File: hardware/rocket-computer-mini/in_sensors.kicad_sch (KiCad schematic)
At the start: 20 parts, among them J8 CON-SMA-EDGE-S, U16 E220-900MM22S, U2 ISM6HG256XTR, U3 IIS2MDCTR, U4 BMP585, U5 LC86GLAMD

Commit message: hardware(minis): cost-reduction part swaps (Tier A + USB-C + QMC5883P)
rocket-computer-mini:
- pyro high-side P-FETs U6-U10: TPN4R712MD -> Winsok WSD20L50DN33 (incumbent
  unbuyable at build qty until the Q4-2026 Mouser restock; land compatibility
  closed by numeric overlay of the vendor package drawing vs the TSON Advance
  land vs the Toshiba outline -- identical 0.202 mm bottom-metal overlap;
  first-article gate: end-face wetting + bench-fire)
- pyro-ARM N-FET U9: CSD16323Q3 -> AOS AON7534 (same pinout, land verified)
- gate drivers Q3-Q6: DTC123JEBTL -> DTC123JETL (SOT-416 leads land fully)
- battery shunt R72: CSSH0805FT2L00 -> Yageo PA0805FRF870R002L
- magnetometer U3: IIS2MDC -> QST QMC5883P (new Custom symbol + LGA-16 3x3
  footprint from the vendor land; U3 relocated, C2/C4/C6 re-arranged; C6
  220 nF -> 4.7 uF 16 V 0603 for the C1 reservoir; 2x2 mm all-layer no-pour
  rule area under the die; stale X/Y axis silk removed -- new markings when
  the firmware axis mapping is decided; needs a new ~10-register driver)
- USB-C stays GCT: the HRO's through-hole shell legs land inside the pyro
  terminal's back-side SMD pads -- physically blocked at this location

base-station-mini:
- USB-C J2: GCT USB4110-GF-A -> HRO TYPE-C-31-M-12 (project footprint with
  symbol-matched pad names; NPTH-aligned placement, mating face within
  0.03 mm of the GCT; R14/R15 nudged 1.0 mm, one GND via moved, VBUS
  re-bridged; DRC 0 unconnected / 0 parity; shell-leg holes must be fully
  filled with solder at assembly)
- thermistor TH1: 103AT-2 -> MF52B 103F3435-100 (beta 3435 matched, charger
  TS window unchanged)
- LEDs D6/D9: Kingbright -> Xinglight

both minis:
- 22 uF 0805: CL21A226MOQNNNE -> CL21A226KOQNNNE (tighter K tolerance)
- bom.csv regenerated from the schematics; TSON footprint tags updated

Verification: rocket-mini ERC one error better than baseline, DRC 246
unconnected (3 better), parity equal, no new errors; base-mini ERC unchanged,
DRC clean.

Co-Authored-By: Cla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
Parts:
- C23, C37: MPN CL21A226MOQNNNE -> CL21A226KOQNNNE
- C6: value 220 nF -> 4.7 uF; footprint Capacitor_SMD:C_0402_1005Metric -> Capacitor_SMD:C_0603_1608Metric; MPN CL05B224KO5NNNC -> CL10A475KO8NNNC
- U3: value IIS2MDCTR -> QMC5883P; footprint Footprints:LGA-12_2X2X0P7_STM -> Footprints:QMC5883P_LGA-16_3x3; symbol Custom:IIS2MDCTR -> Custom:QMC5883P; MPN IIS2MDCTR -> QMC5883P; Mfr STMicro -> QST
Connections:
- net GND: now also U3.11 (GND), U3.9 (GND); no longer U3.6 (GND), U3.8 (GND)
- net SEN_SDA: now also U3.16 (SDA); no longer U3.4 (SDA/SDI/SDO)
- net V_MCU_SWTCH: now also U3.2 (VDD); no longer U3.10 (VDD_IO), U3.3 (CS), U3.9 (VDD)
- net at C6.1: now also U3.10 (C1); no longer U3.5 (C1)
- net at U3.7 (NC): now also U3.12 (NC), U3.13 (NC), U3.14 (NC), U3.15 (NC), U3.3 (NC), U3.4 (NC), U3.5 (NC), U3.6 (NC), U3.8 (NC)
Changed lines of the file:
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@@
 		)
 	)
-	(wire
-		(pts
-			(xy 46.355 41.91) (xy 46.355 44.45)
-		)
-		(stroke
-			(width 0)
-			(type default)
-		)
-	)
-	(wire
+		(wire
 		(pts
 			(xy 252.095 45.72) (xy 264.795 45.72)
@@
 		)
 	)
-	(wire
-		(pts
-			(xy 46.355 44.45) (xy 46.355 46.99)
-		)
-		(stroke
-			(width 0)
-			(type default)
-		)
-	)
-	(wire
+		(wire
 		(pts
 			(xy 85.725 49.53) (xy 85.725 52.07)
@@
 			)
 		)
-		(property "Value" "220 nF"
+		(property "Value" "4.7 uF"
 			(at 94.615 50.8 0)
 			(show_name no)
@@
 			)
 		)
-		(property "Footprint" "Capacitor_SMD:C_0402_1005Metric"
+		(property "Footprint" "Capacitor_SMD:C_0603_1608Metric"
 			(at 95.5802 52.07 0)
 			(hide yes)
@@
 			)
 		)
-		(property "MPN" "CL05B224KO5NNNC"
+		(property "MPN" "CL10A475KO8NNNC"
 			(at 94.615 48.26 0)
 			(hide yes)
@@
 	)
 	(symbol
-		(lib_id "Custom:IIS2MDCTR")
+		(lib_id "Custom:QMC5883P")
 		(at 65.405 45.72 0)
 		(unit 1)
@@
 			)
 		)
-		(property "Value" "IIS2MDCTR"
+		(property "Value" "QMC5883P"
 			(at 66.04 36.83 0)
 			(show_name no)
@@
 			)
 		)
-		(property "Footprint" "Footprints:LGA-12_2X2X0P7_STM"
+		(property "Footprint" "Footprints:QMC5883P_LGA-16_3x3"
 			(at 79.883 31.496 0)
 			(hide yes)
@@
 			)
 		)
-		(property "Datasheet" "https://www.st.com/resource/en/datasheet/iis2mdc.pdf"
+		(property "Datasheet" "QMC5883P"
 			(at 76.073 28.956 0)
 			(hide yes)
@@
 			)
 		)
-		(property "MPN" "IIS2MDCTR"
+		(property "MPN" "QMC5883P"
 			(at 65.405 45.72 0)
 			(hide yes)
@@
 			)
 		)
-		(property "Mfr" "STMicro"
+		(property "Mfr" "QST"
 			(at 65.405 45.72 0)
 			(hide yes)
@@
 			)
 		)
-		(pin "2"
+		(pin "1"
 		)
-		(pin "5"
+		(pin "16"
 		)
-		(pin "11"
+		(pin "2"
 		)
-		(pin "12"
+		(pin "10"
 		)
 		(pin "9"
 		)
-		(pin "1"
+		(pin "11"
 		)
-		(pin "7"
+		(pin "3"
+		)
+		(pin "4"
+		)
+		(pin "5"
 		)
 		(pin "6"
 		)
+		(pin "7"
+		)
 		(pin "8"
 		)
-		(pin "4"
+		(pin "12"
 		)
-		(pin "3"
+		(pin "13"
 		)
-		(pin "10"
+		(pin "14"
+		)
+		(pin "15"
 		)
 		(instances
@@
 			)
 		)
-		(property "MPN" "CL21A226MOQNNNE"
+		(property "MPN" "CL21A226KOQNNNE"
 			(at 207.645 102.87 0)
 			(hide yes)
@@
 			)
 		)
-		(property "MPN" "CL21A226MOQNNNE"
+		(property "MPN" "CL21A226KOQNNNE"
 			(at 191.77 41.91 0)
 			(hide yes)

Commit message: hardware(rocket-computer-mini): barometer BMP585 -> BMP581
Same BMP5 sensor API/register map, so no firmware change; SPI wiring maps
1:1 (SCK/SDI/SDO/CSB/INT; VDD+VDDIO on the switched sensor rail; three VSS
pins stacked at the old GND pin position so existing wires are untouched).

- new Custom:BMP581 symbol (shared lib + sheet cache)
- new footprint Footprints:BMP581_LGA-10_2x2 from the vendor land - the 581
  is an LGA-10 2.0x2.0 vs the 585's 9-pad 3.25x3.25, so U4's footprint is
  replaced in place; placement/routing tidy-up belongs to the layout pass
- trade-off taken on: no gel fill / liquid resistance; the baro drives
  apogee detection, so bench-compare noise vs a 585 at first article
- bom.csv regenerated

ERC unchanged vs pre-swap; DRC parity at baseline, no new errors.

Co-Authored-By: Claude Fable 5 <noreply@anthropic.com>
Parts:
- U4: value BMP585 -> BMP581; footprint Footprints:LGA9_BMP585_BOS -> Footprints:BMP581_LGA-10_2x2; symbol Custom:BMP585 -> Custom:BMP581; MPN BMP585 -> BMP581
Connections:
- net BMP585_CS: now also U4.6 (CSB); no longer U4.7 (CSB)
- net BMP585_INT: now also U4.7 (INT); no longer U4.5 (INT)
- net GND: now also U4.3 (VSS), U4.8 (VSS), U4.9 (VSS); no longer U4.6 (VSS)
- net SENS_SCLK: now also U4.2 (SCK); no longer U4.1 (SCX)
- net SENS_SDI: now also U4.4 (SDI); no longer U4.2 (SDX)
- net SENS_SDO: now also U4.5 (SDO); no longer U4.3 (SDO)
- net V_MCU_SWTCH: now also U4.1 (VDDIO), U4.10 (VDD); no longer U4.4 (VDDIO), U4.8 (VDD)
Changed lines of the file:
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@@
 	)
 	(symbol
-		(lib_id "Custom:BMP585")
+		(lib_id "Custom:BMP581")
 		(at 66.04 102.235 0)
 		(unit 1)
@@
 			)
 		)
-		(property "Value" "BMP585"
+		(property "Value" "BMP581"
 			(at 66.04 93.98 0)
 			(show_name no)
@@
 			)
 		)
-		(property "Footprint" "Footprints:LGA9_BMP585_BOS"
+		(property "Footprint" "Footprints:BMP581_LGA-10_2x2"
 			(at 66.04 102.235 0)
 			(hide yes)
@@
 			)
 		)
-		(property "Datasheet" "BMP585"
+		(property "Datasheet" "BMP581"
 			(at 66.04 102.235 0)
 			(hide yes)
@@
 			)
 		)
-		(property "MPN" "BMP585"
+		(property "MPN" "BMP581"
 			(at 66.04 102.235 0)
 			(hide yes)
@@
 			)
 		)
+		(pin "2"
+		)
+		(pin "5"
+		)
 		(pin "4"
+		)
+		(pin "6"
+		)
+		(pin "10"
+		)
+		(pin "1"
+		)
+		(pin "7"
 		)
 		(pin "3"
 		)
-		(pin "6"
-		)
-		(pin "5"
-		)
-		(pin "1"
-		)
-		(pin "2"
+		(pin "8"
 		)
 		(pin "9"
 		)
-		(pin "8"
-		)
-		(pin "7"
-		)
 		(instances

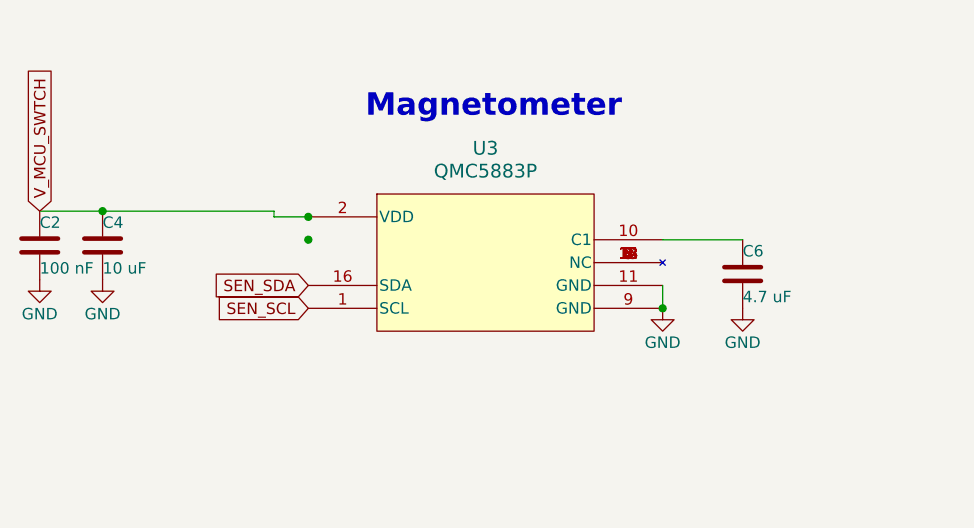
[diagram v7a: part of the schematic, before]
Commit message: hardware(rocket-computer-mini): TDK chip antenna replaces the Molex BLE antenna
U14 (Molex 479480001, on-ground) removed; U31 (TDK ANT016008LCS2442MA2,
1.6x0.8 multilayer) is now the BLE antenna, placed per the layout session at
the bottom-right corner strip:

- keep-out: 2.9 x 6.5 mm all-layer rule area using the board's right and
  bottom edges as two sides (TDK asks 6 x 2.5); GND stitching vias along the
  west boundary
- printed radiator arm ~5.2 mm x 0.6 mm running down the right edge from the
  RAD pin (open end intentional - shows as one dangling-track warning)
- matching per TDK reference: L7 Ft 2.0 nH series + L8 Mt 3.0 nH shunt
  (LQG15 0402, EVAL VALUES - VNA tune on the real board required, S11
  < -10 dB across 2402-2480 MHz + range check vs a Molex board)
- feed: existing L1 4.3 nH shunt at the ESP32 stays; new ~15.5 mm 50-ohm
  stripline on In2 between the In1/In3 ground planes at 0.22 mm width
  (estimate for the default JLCPCB 6-layer JLC06161H-3313 stackup - VERIFY
  with JLCPCB's impedance calculator before ordering, or use their
  controlled-impedance service, In2 pour keep-out corridor, 2 vias with
  local ground return
- R21/R22/R37 relocated into the freed Molex area (clear of the H4 screw
  head courtyard and J3's back-side pads); redundant In2 GND stitching in
  the corridor removed
- C6 (QMC C1 reservoir) consolidated onto the stock 10 uF 0402 line per the
  owner's edit; the dedicated 4.7 uF line is gone
- schematic: ANT_FEED chain U15.RF + L1 -> Mt/Ft -> U31; U14 deleted

Verification: ERC 4 errors better than the session baseline; DRC zero new
errors, parity unchanged (1 pre-existing cosmetic), unconnected one better;
BOM reconciles with the curated cross-board sheet line-for-line. Known
cosmetics: radiator open-end dangling (by design), one 0.47 mm2 floating
In2 fill sliver (set zone island-removal or ignore), L7/L8 silk refs over
own pads.

Co-Authored-By: Claude Fable 5 <noreply@anthropic.com>
EOF
)
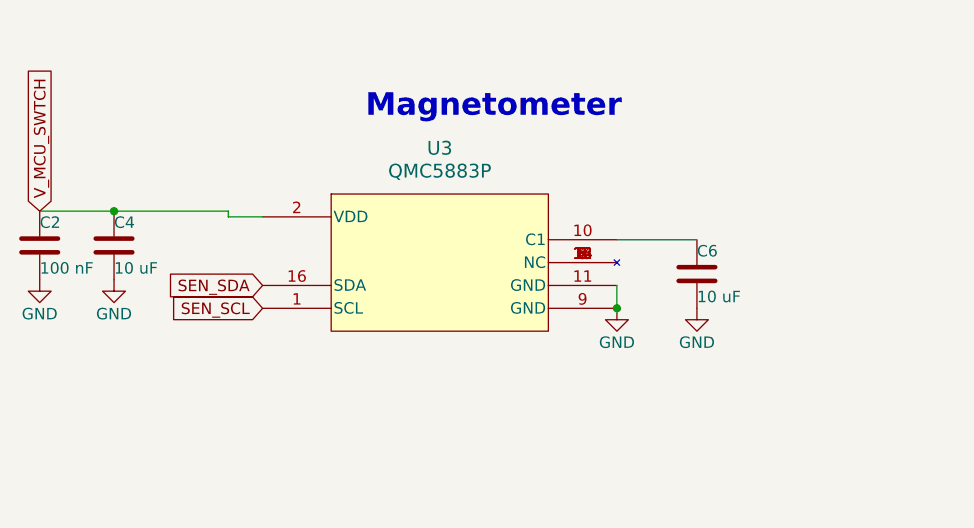
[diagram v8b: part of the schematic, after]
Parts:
- C6: value 4.7 uF -> 10 uF; footprint Capacitor_SMD:C_0603_1608Metric -> Capacitor_SMD:C_0402_1005Metric; MPN CL10A475KO8NNNC -> CL05A106MQ5NUNC
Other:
- moved on the sheet: C4, U3
